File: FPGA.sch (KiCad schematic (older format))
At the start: 23 parts, among them U24 ICE40HX1K-4K-TQ144

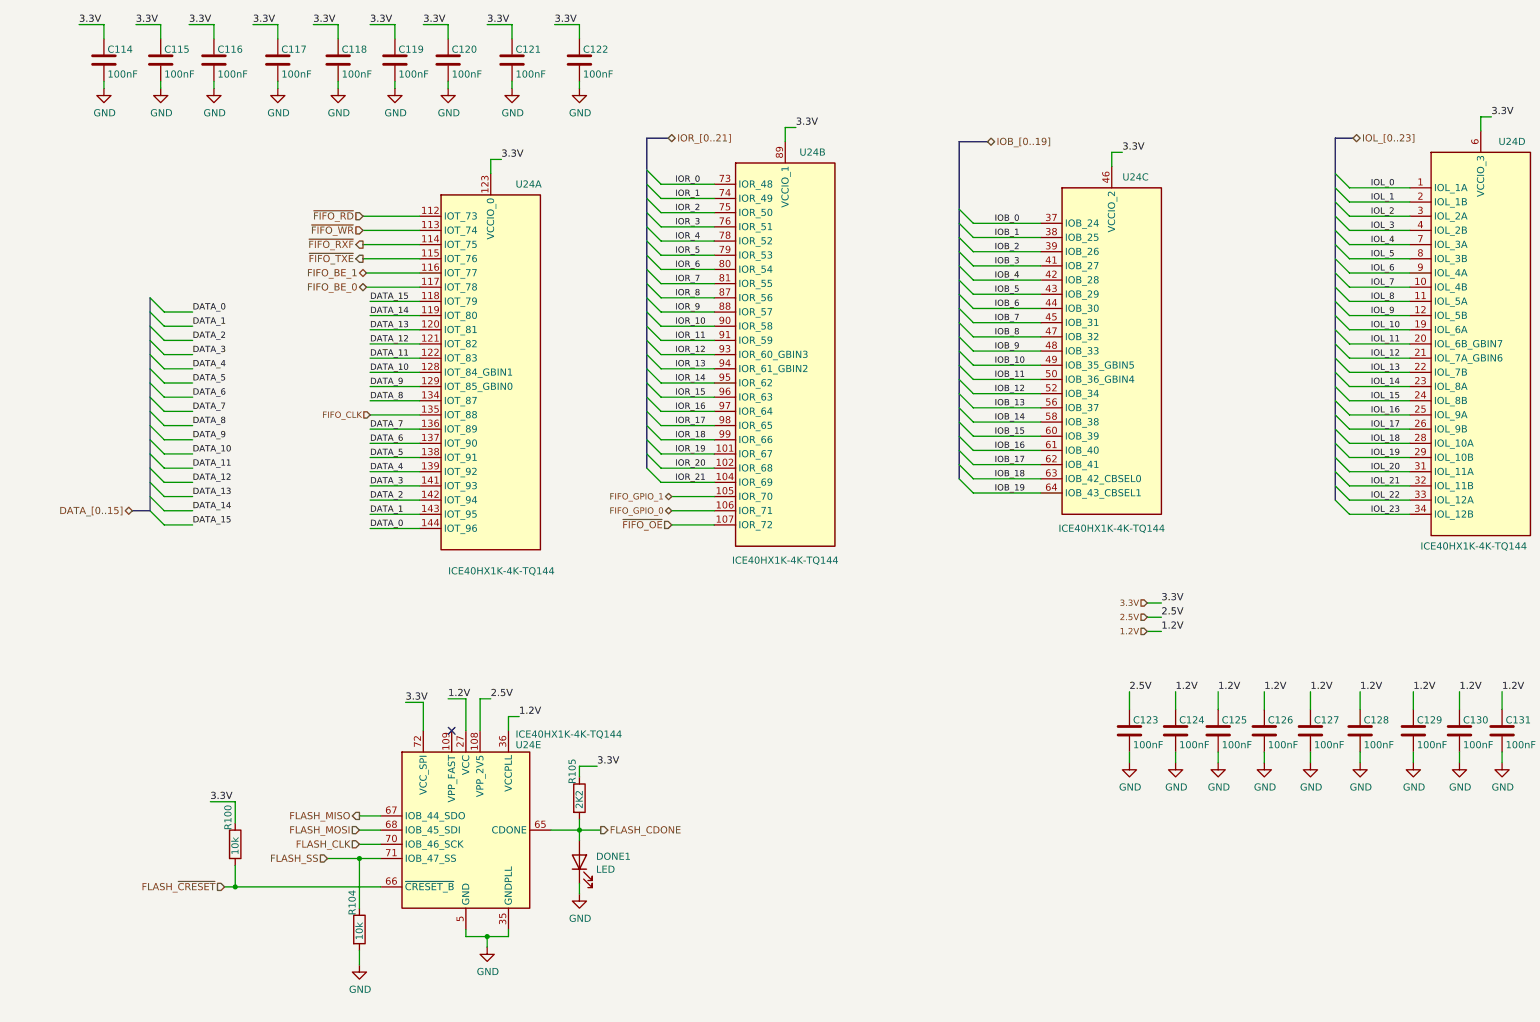
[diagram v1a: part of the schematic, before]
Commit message: Layout done for ADC + LVDS and DAC -> FPGA
Signed-off-by: Alexis Jeandet <alexis.jeandet@member.fsf.org>
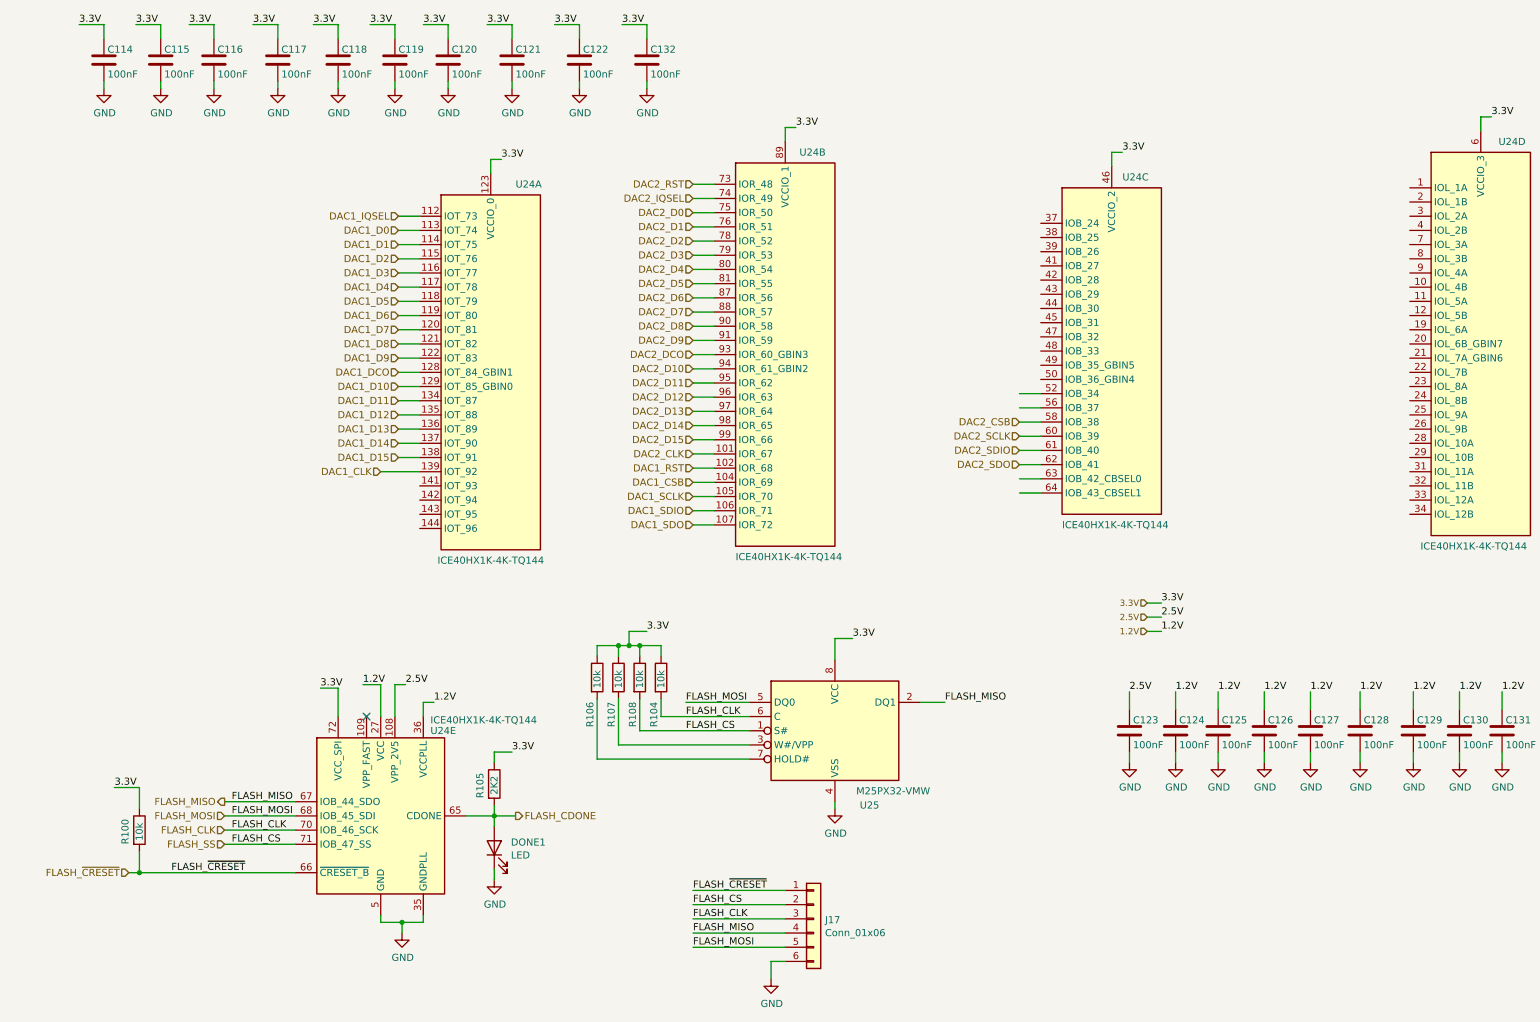
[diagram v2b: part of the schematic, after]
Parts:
- added C132: 100nF, Capacitor_SMD:C_0402_1005Metric, symbol Device:C
- added J17: Conn_01x06, Connector_PinHeader_2.54mm:PinHeader_1x06_P2.54mm_Vertical, symbol Connector_Generic:Conn_01x06
- added R106, R107, R108: 10k, Resistor_SMD:R_0402_1005Metric, symbol Device:R
- added U25: M25PX32-VMW, Package_SO:SOIJ-8_5.3x5.3mm_P1.27mm, symbol Memory_Flash:M25PX32-VMW
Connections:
- net FLASH_CLK: now also R401.2, J17.3 (Pin_3), U25.6 (C)
- net FLASH_MISO: now also J17.4 (Pin_4), U25.2 (DQ1)
- net FLASH_MOSI: now also J17.5 (Pin_5), U25.5 (DQ0)
- net FLASH_SS: now also J17.2 (Pin_2), R108.2, U25.1 (S#); no longer R401.1
- net FLASH_~CRESET: now also J17.1 (Pin_1)
- net GND: now also C132.2, J17.6 (Pin_6), U25.4 (VSS); no longer R401.2
- net VCCIO_0: now also R401.1, C132.1, R106.1, R107.1, R108.1, U25.8 (VCC)
- net DATA_0: no longer names the net of U24.144 (IOT_96)
- net DATA_1: no longer names the net of U24.143 (IOT_95)
- net DATA_10 renamed DAC1_DCO
- net DATA_11 renamed DAC1_D9
- net DATA_12 renamed DAC1_D8
- net DATA_13 renamed DAC1_D7
- net DATA_14 renamed DAC1_D6
- net DATA_15 renamed DAC1_D5
- net DATA_2: no longer names the net of U24.142 (IOT_94)
- net DATA_3: no longer names the net of U24.141 (IOT_93)
- net DATA_4 renamed DAC1_CLK
- net DATA_5 renamed DAC1_D15
- net DATA_6 renamed DAC1_D14
- net DATA_7 renamed DAC1_D13
- net DATA_8 renamed DAC1_D11
- net DATA_9 renamed DAC1_D10
- net FIFO_BE_0 renamed DAC1_D4
- net FIFO_BE_1 renamed DAC1_D3
- net FIFO_CLK renamed DAC1_D12
- net FIFO_GPIO_0 renamed DAC1_SDIO
- net FIFO_GPIO_1 renamed DAC1_SCLK
- net IOB_0: no longer names the net of U24.37 (IOB_24)
- net IOB_1: no longer names the net of U24.38 (IOB_25)
- net IOB_10: no longer names the net of U24.49 (IOB_35_GBIN5)
- net IOB_11: no longer names the net of U24.50 (IOB_36_GBIN4)
- net IOB_12: no longer names the net of U24.52 (IOB_34)
- net IOB_13: no longer names the net of U24.56 (IOB_37)
- net IOB_14 renamed DAC2_CSB
- net IOB_15 renamed DAC2_SCLK
- net IOB_16 renamed DAC2_SDIO
- net IOB_17 renamed DAC2_SDO
- net IOB_18: no longer names the net of U24.63 (IOB_42_CBSEL0)
- net IOB_19: no longer names the net of U24.64 (IOB_43_CBSEL1)
- net IOB_2: no longer names the net of U24.39 (IOB_26)
- net IOB_3: no longer names the net of U24.41 (IOB_27)
- net IOB_4: no longer names the net of U24.42 (IOB_28)
- net IOB_5: no longer names the net of U24.43 (IOB_29)
- net IOB_6: no longer names the net of U24.44 (IOB_30)
- net IOB_7: no longer names the net of U24.45 (IOB_31)
- net IOB_8: no longer names the net of U24.47 (IOB_32)
- net IOB_9: no longer names the net of U24.48 (IOB_33)
- net IOL_0: no longer names the net of U24.1 (IOL_1A)
- net IOL_1: no longer names the net of U24.2 (IOL_1B)
- net IOL_10: no longer names the net of U24.19 (IOL_6A)
- net IOL_11: no longer names the net of U24.20 (IOL_6B_GBIN7)
- net IOL_12: no longer names the net of U24.21 (IOL_7A_GBIN6)
- net IOL_13: no longer names the net of U24.22 (IOL_7B)
- net IOL_14: no longer names the net of U24.23 (IOL_8A)
- net IOL_15: no longer names the net of U24.24 (IOL_8B)
- net IOL_16: no longer names the net of U24.25 (IOL_9A)
- net IOL_17: no longer names the net of U24.26 (IOL_9B)
- net IOL_18: no longer names the net of U24.28 (IOL_10A)
- net IOL_19: no longer names the net of U24.29 (IOL_10B)
- net IOL_2: no longer names the net of U24.3 (IOL_2A)
- net IOL_20: no longer names the net of U24.31 (IOL_11A)
- net IOL_21: no longer names the net of U24.32 (IOL_11B)
- net IOL_22: no longer names the net of U24.33 (IOL_12A)
- net IOL_23: no longer names the net of U24.34 (IOL_12B)
- net IOL_3: no longer names the net of U24.4 (IOL_2B)
- net IOL_4: no longer names the net of U24.7 (IOL_3A)
- net IOL_5: no longer names the net of U24.8 (IOL_3B)
- net IOL_6: no longer names the net of U24.9 (IOL_4A)
- net IOL_7: no longer names the net of U24.10 (IOL_4B)
- net IOL_8: no longer names the net of U24.11 (IOL_5A)
- net IOL_9: no longer names the net of U24.12 (IOL_5B)
- net IOR_0 renamed DAC2_RST
- net IOR_1 renamed DAC2_IQSEL
- net IOR_10 renamed DAC2_D8
- net IOR_11 renamed DAC2_D9
- net IOR_12 renamed DAC2_DCO
- net IOR_13 renamed DAC2_D10
- net IOR_14 renamed DAC2_D11
- net IOR_15 renamed DAC2_D12
- net IOR_16 renamed DAC2_D13
- net IOR_17 renamed DAC2_D14
- net IOR_18 renamed DAC2_D15
- net IOR_19 renamed DAC2_CLK
- net IOR_2 renamed DAC2_D0
- net IOR_20 renamed DAC1_RST
- net IOR_21 renamed DAC1_CSB
- net IOR_3 renamed DAC2_D1
- net IOR_4 renamed DAC2_D2
- net IOR_5 renamed DAC2_D3
- net IOR_6 renamed DAC2_D4
- net IOR_7 renamed DAC2_D5
- net IOR_8 renamed DAC2_D6
- net IOR_9 renamed DAC2_D7
- net ~FIFO_OE renamed DAC1_SDO
- net ~FIFO_RD renamed DAC1_IQSEL
- net ~FIFO_RXF renamed DAC1_D1
- net ~FIFO_TXE renamed DAC1_D2
- net ~FIFO_WR renamed DAC1_D0
- new net: R107.2, U25.3 (W#/VPP)
- new net: R106.2, U25.7 (HOLD#)
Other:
- moved on the sheet: DONE1, R100, R104, R105, U24E

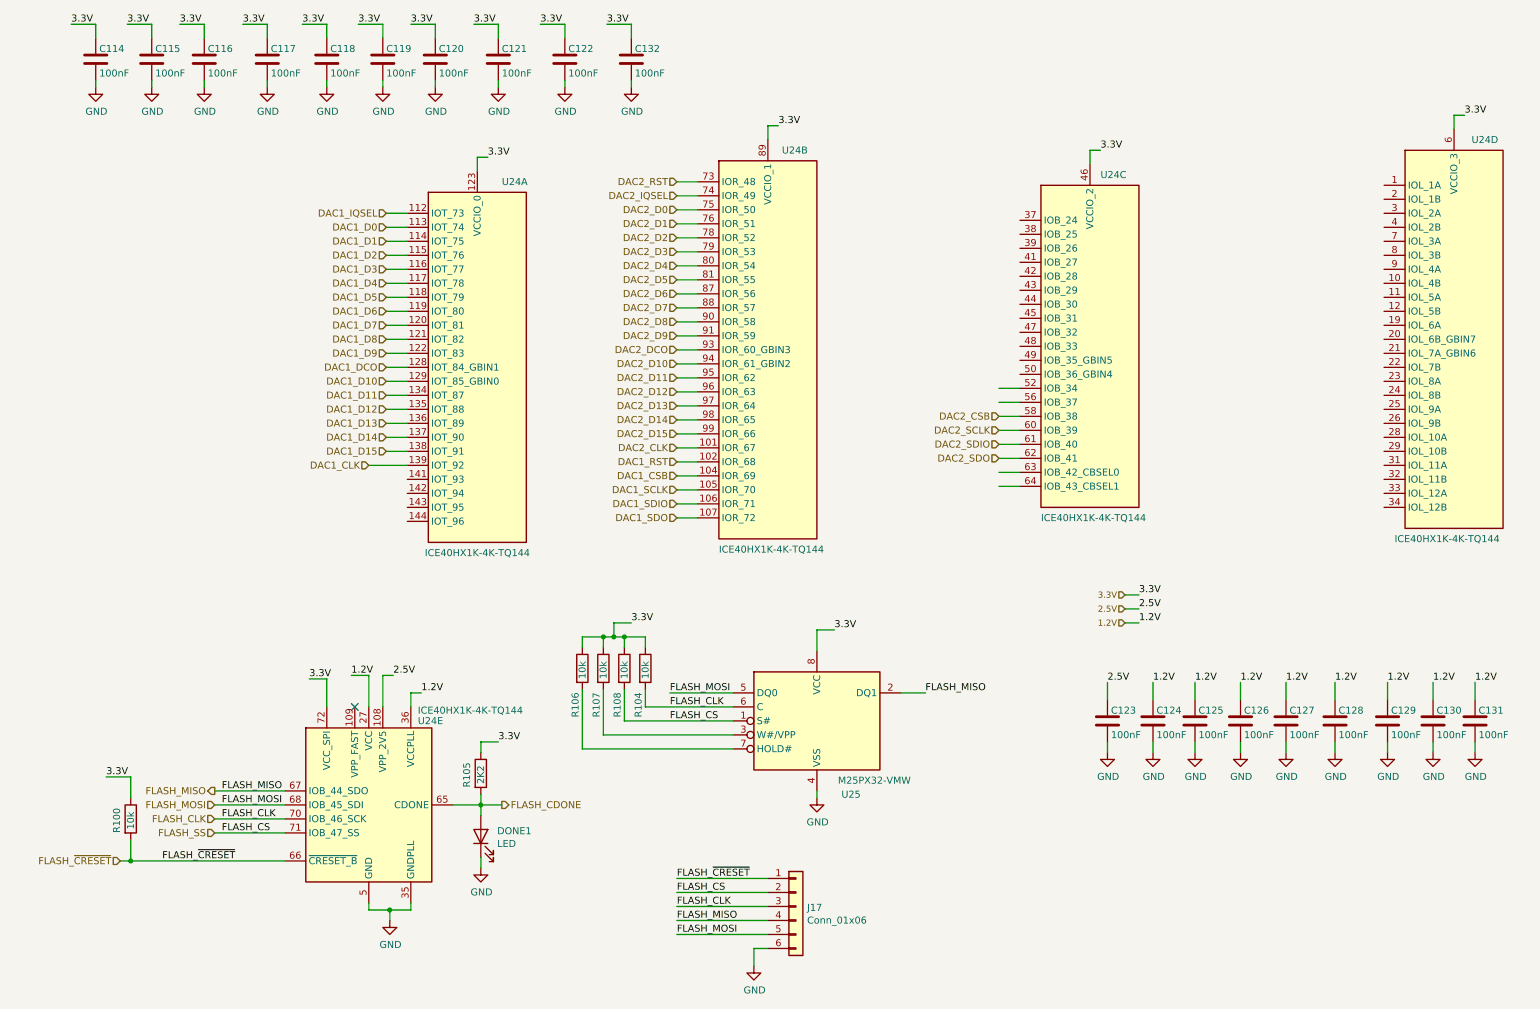
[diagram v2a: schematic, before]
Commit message: Added #3.3V and #1.2V supply, completed ADC to USB board layout, added DAC FPGA to USB board bus.
Signed-off-by: Alexis Jeandet <alexis.jeandet@member.fsf.org>
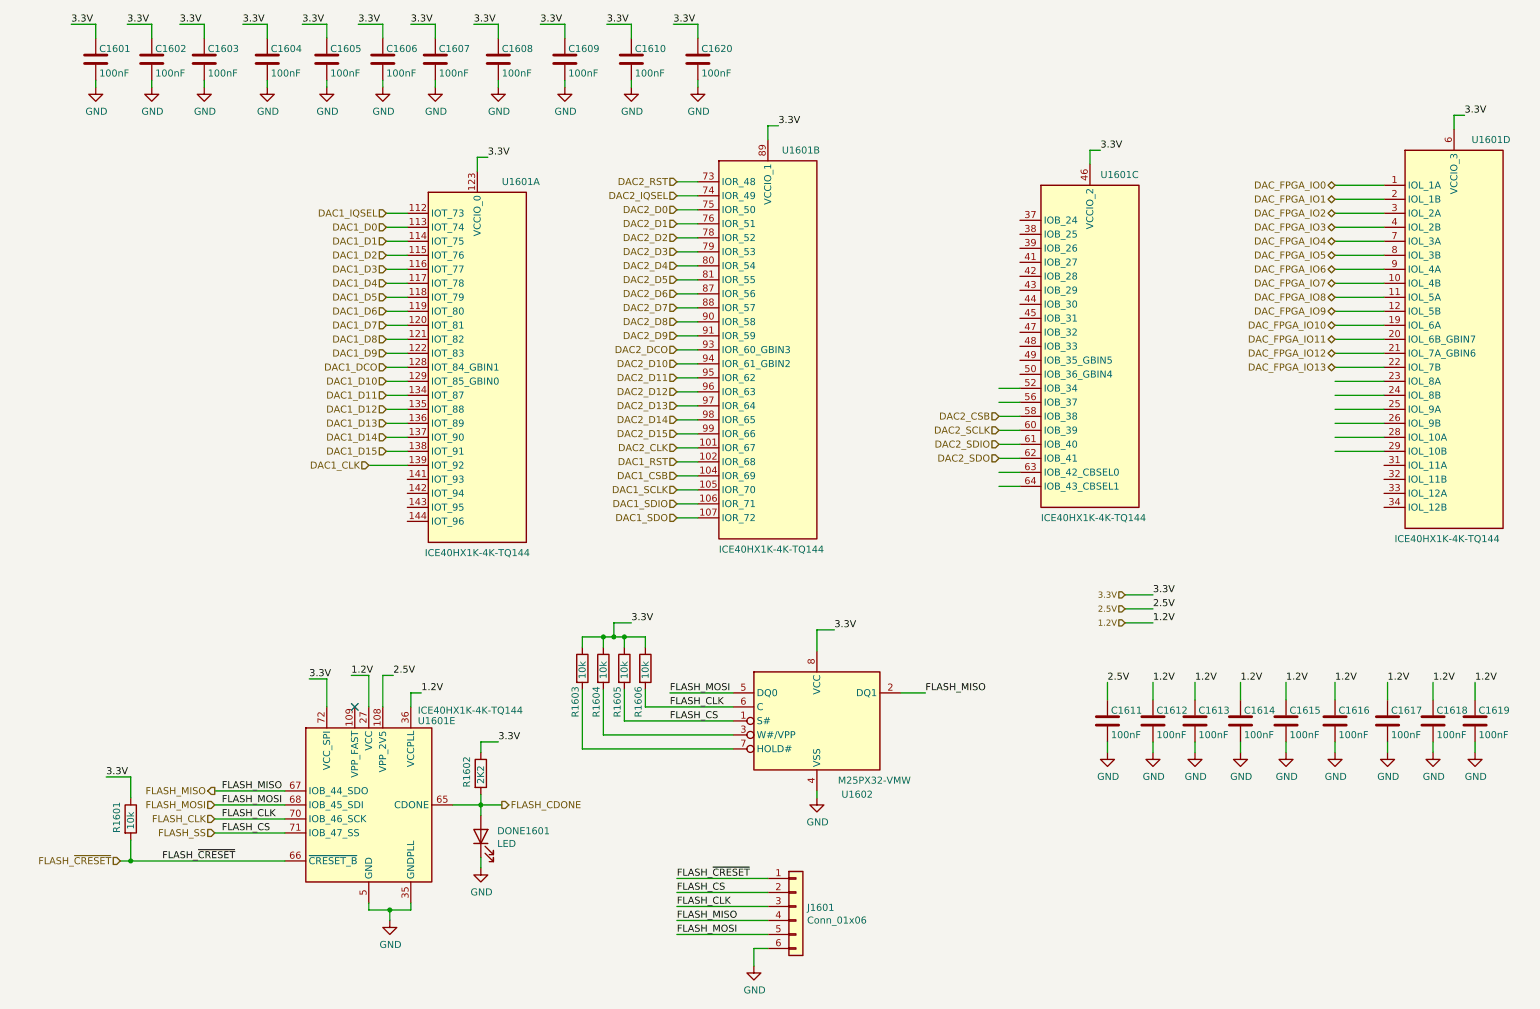
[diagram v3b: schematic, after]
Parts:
- added C1620: 100nF, Capacitor_SMD:C_0402_1005Metric, symbol Device:C
- renumbered C301 to C1601, C302 to C1602, C303 to C1603, C308 to C1604, C309 to C1605, C310 to C1606, C311 to C1607, C312 to C1608, C316 to C1609, C132 to C1610, C305 to C1611, C306 to C1612, C307 to C1613, C313 to C1614, C314 to C1615, C315 to C1616, C317 to C1617, C318 to C1618, C319 to C1619, DONE401 to DONE1601, J17 to J1601, R305 to R1601, R306 to R1602, R106 to R1603, R107 to R1604, R108 to R1605, R401 to R1606, U24 to U1601, U25 to U1602
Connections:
- net labels added: DAC_FPGA_IO0, DAC_FPGA_IO1, DAC_FPGA_IO10, DAC_FPGA_IO11, DAC_FPGA_IO12, DAC_FPGA_IO13, DAC_FPGA_IO2, DAC_FPGA_IO3, DAC_FPGA_IO4, DAC_FPGA_IO5, DAC_FPGA_IO6, DAC_FPGA_IO7, DAC_FPGA_IO8, DAC_FPGA_IO9
- wire segments 170 -> 193

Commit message: Layout complete, needs silk screen cleanup and few checks
Signed-off-by: Alexis Jeandet <alexis.jeandet@member.fsf.org>
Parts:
- added C1621, C1622: 100nF, Capacitor_SMD:C_0402_1005Metric, symbol Device:C
- added D1601, D1602: LED, Resistor_SMD:R_0603_1608Metric_Pad1.05x0.95mm_HandSolder, symbol Device:LED
- added R1607, R1608, R1609: 2K2, Resistor_SMD:R_0402_1005Metric, symbol Device:R
- added SW1601: SW_Push, Button_Switch_SMD:SW_SPST_EVQPE1, symbol Switch:SW_Push
- added U1603: ASDMB-xxxMHz, Oscillator:Oscillator_SMD_Abracon_ASDMB-4Pin_2.5x2.0mm, symbol Oscillator:ASDMB-xxxMHz
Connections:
- net labels added: BP, FPGA_CLK, LED1, LED2
- wire segments 193 -> 225
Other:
- moved on the sheet: DONE1601, R1601, R1602, U1601E
